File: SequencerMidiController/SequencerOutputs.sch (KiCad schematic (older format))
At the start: 30 parts, among them J4 Conn_02x10_Odd_Even, SW2 SW_DIP_x04, SW7 SW_SPST, U34 ADG2188

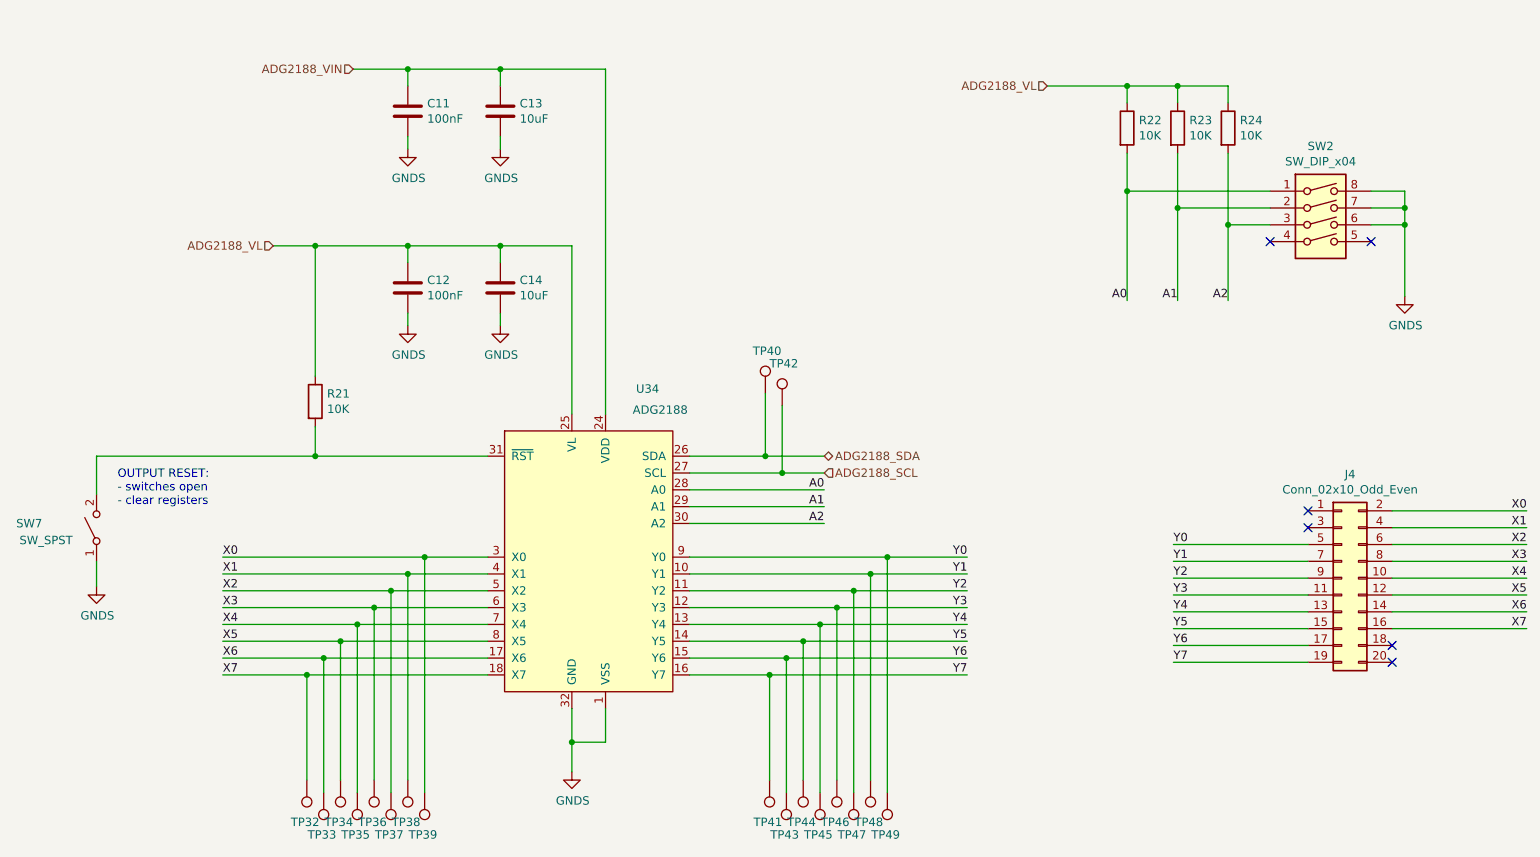
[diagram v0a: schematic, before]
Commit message: RevA Layout draft completed
- Needs tidy up
- Add test points
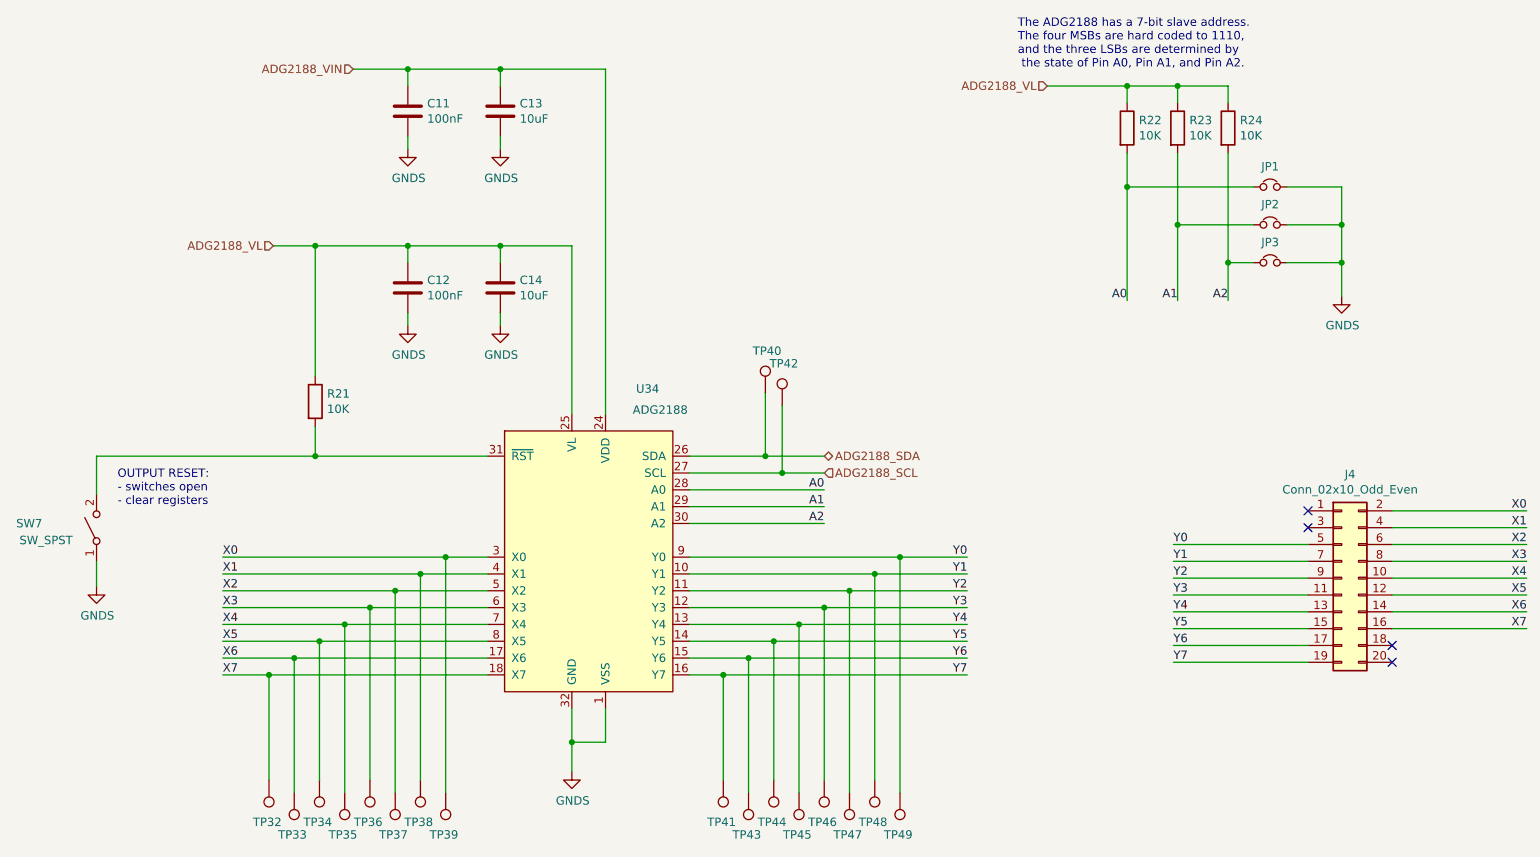
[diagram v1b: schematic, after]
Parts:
- removed SW2: SW_DIP_x04, Button_Switch_THT:SW_DIP_SPSTx04_Slide_9.78x12.34mm_W7.62mm_P2.54mm, symbol Switch:SW_DIP_x04
- added JP1, JP2, JP3: Jumper_NC_Small, Jumper:SolderJumper-2_P1.3mm_Bridged_RoundedPad1.0x1.5mm, symbol Device:Jumper_NC_Small
- J4: footprint Connector_PinHeader_2.54mm:PinHeader_2x10_P2.54mm_Vertical -> Connector_IDC:IDC-Header_2x10_P2.54mm_Horizontal
- SW7: footprint Button_Switch_THT:SW_TH_Tactile_Omron_B3F-10xx -> Button_Switch_THT:SW_PUSH-12mm
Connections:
- net A0: now also JP1.1
- net A1: now also JP2.1
- net A2: now also JP3.1
- net GNDS: now also JP1.2, JP2.2, JP3.2
- no-connect marks 6 -> 4
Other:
- note added: "The ADG2188 has a 7-bit slave address. \nThe four MSBs are hard coded to 1110, \nand the three LSBs are determined by\n the state of Pin A0, Pin A1, and Pin A2."
- moved on the sheet: TP32, TP33, TP34, TP35, TP36, TP37, TP38, TP39, TP41, TP43, TP44, TP45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
